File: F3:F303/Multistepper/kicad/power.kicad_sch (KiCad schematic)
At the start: 22 parts, among them J10 Screw_Terminal_01x02, Q2 IRF9310, U4 LM4050A(b)EX3-3.3, U5 LM2576-5.0, U6 LM1117-3.3

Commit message: multistepper: cont
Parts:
- added JP4, JP5: SolderJumper_2_Bridged, Jumper:SolderJumper-2_P1.3mm_Open_TrianglePad1.0x1.5mm, symbol Jumper:SolderJumper_2_Bridged
- C13, C15, C18: footprint Capacitor_SMD:C_0603_1608Metric_Pad1.05x0.95mm_HandSolder -> Capacitor_SMD:C_0603_1608Metric_Pad1.08x0.95mm_HandSolder
- R19, R20: footprint Resistor_SMD:R_0603_1608Metric_Pad1.05x0.95mm_HandSolder -> Resistor_SMD:R_0603_1608Metric_Pad0.98x0.95mm_HandSolder
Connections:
- net +5V: now also JP4.1 (A), JP5.1 (A); no longer C15.1, R20.2, U6.3 (VI)
- new net: C15.1, JP5.2 (B), U6.3 (VI)
- new net: JP4.2 (B), R20.2
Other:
- moved on the sheet: C12, R20, U4

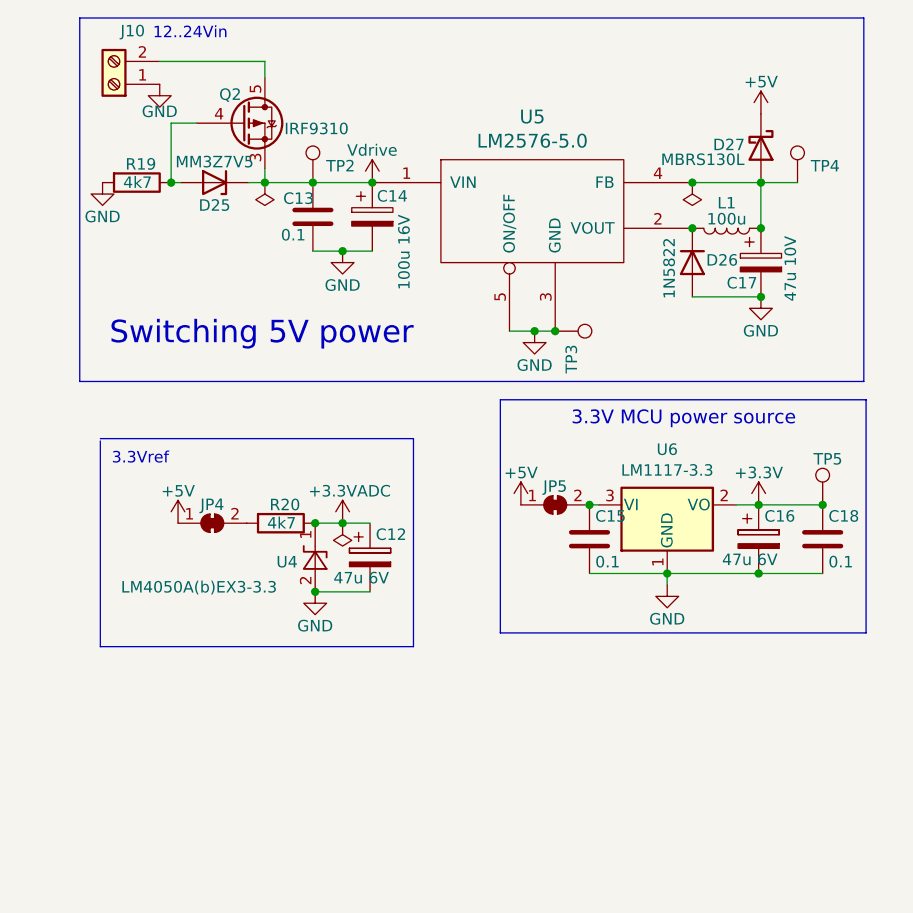
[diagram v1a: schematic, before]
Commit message: Multistepper PCB almost ready
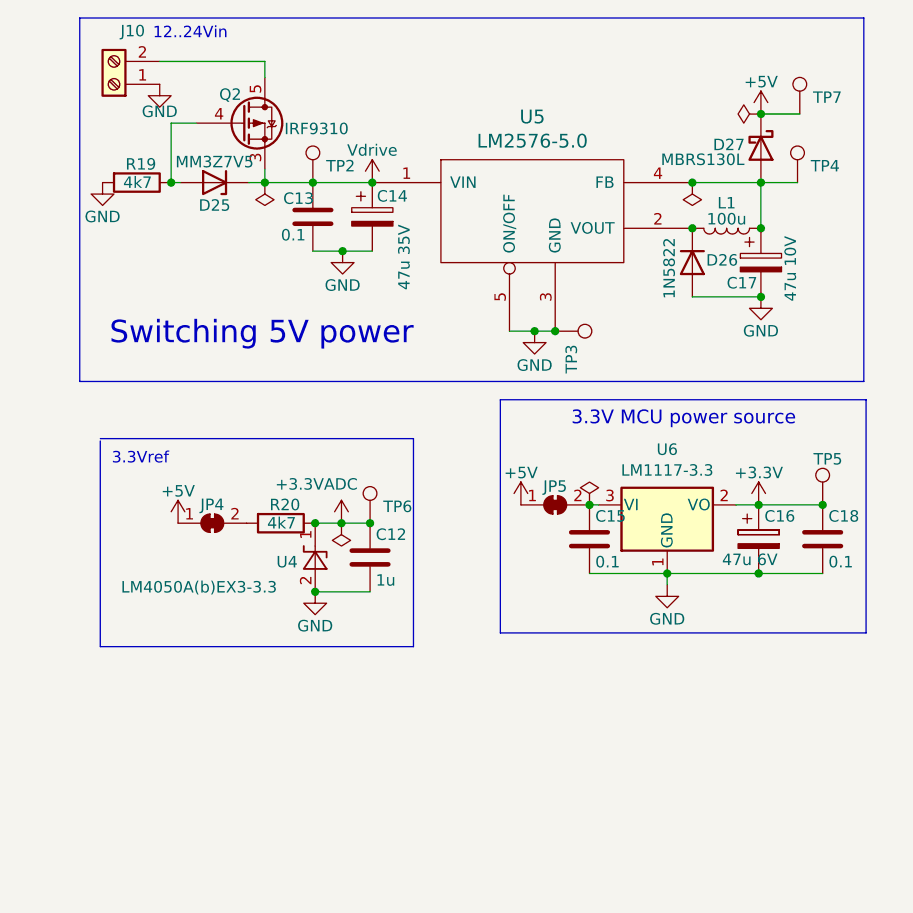
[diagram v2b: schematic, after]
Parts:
- removed C12: 47u 6V, Capacitor_Tantalum_SMD:CP_EIA-3216-18_Kemet-A_Pad1.58x1.35mm_HandSolder, symbol stm32-rescue:CP
- added C12: 1u, Capacitor_SMD:C_0603_1608Metric_Pad1.08x0.95mm_HandSolder, symbol stm32-rescue:C
- added TP6: 3V3ADC, TestPoint:TestPoint_THTPad_1.5x1.5mm_Drill0.7mm, symbol Connector:TestPoint
- added TP7: 5V, TestPoint:TestPoint_THTPad_1.5x1.5mm_Drill0.7mm, symbol Connector:TestPoint
- C14: value 100u 16V -> 47u 35V; footprint Capacitor_THT:CP_Radial_D8.0mm_P3.50mm -> Capacitor_Tantalum_SMD:CP_EIA-6032-28_Kemet-C_Pad2.25x2.35mm_HandSolder
- JP4: value SolderJumper_2_Bridged -> 3V3ADC
- JP5: value SolderJumper_2_Bridged -> 3V3
- TP2: value 5V -> Vin
- TP4: value 5V -> 5Vext
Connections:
- net +3.3VADC: now also C12.1, TP6.1
- net +5V: now also TP7.1
- net GND: now also C12.2
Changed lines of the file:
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@@
   (junction (at 87.376 36.068) (diameter 0) (color 0 0 0 0)
   )
+  (junction (at 48.387 73.914) (diameter 0) (color 0 0 0 0)
+  )
   (junction (at 29.464 36.068) (diameter 0) (color 0 0 0 0)
   )
@@
   (junction (at 51.816 36.068) (diameter 0) (color 0 0 0 0)
   )
-  (junction (at 48.514 73.914) (diameter 0) (color 0 0 0 0)
+  (junction (at 51.562 73.914) (diameter 0) (color 0 0 0 0)
   )
   (junction (at 84.582 79.502) (diameter 0) (color 0 0 0 0)
@@
   (junction (at 48.514 43.688) (diameter 0) (color 0 0 0 0)
   )
+  (junction (at 94.996 28.448) (diameter 0) (color 0 0 0 0)
+  )
   (junction (at 87.376 41.148) (diameter 0) (color 0 0 0 0)
   )
@@
     (stroke (width 0) (type default) (color 0 0 0 0))
   )
-  (wire (pts (xy 51.562 73.914) (xy 48.514 73.914))
+  (wire (pts (xy 45.466 73.914) (xy 48.387 73.914))
     (stroke (width 0) (type default) (color 0 0 0 0))
   )
@@
     (stroke (width 0) (type default) (color 0 0 0 0))
   )
-  (wire (pts (xy 48.514 73.914) (xy 48.514 73.66))
+  (wire (pts (xy 99.314 28.448) (xy 94.996 28.448))
     (stroke (width 0) (type default) (color 0 0 0 0))
   )
@@
     (stroke (width 0) (type default) (color 0 0 0 0))
   )
-  (wire (pts (xy 45.466 73.914) (xy 48.514 73.914))
+  (wire (pts (xy 48.387 73.914) (xy 51.562 73.914))
     (stroke (width 0) (type default) (color 0 0 0 0))
   )
@@
   (text "12..24Vin" (at 27.432 20.32 0)
     (effects (font (size 1.27 1.27)) (justify left bottom))
-  )
-  (symbol (lib_id "stm32-rescue:CP") (at 51.562 77.724 0) (unit 1)
-    (in_bom yes) (on_board yes)
-    (property "Reference" "C12" (id 0) (at 52.197 75.184 0)
-      (effects (font (size 1.27 1.27)) (justify left))
-    )
-    (property "Value" "47u 6V" (id 1) (at 47.498 80.01 0)
-      (effects (font (size 1.27 1.27)) (justify left))
-    )
-    (property "Footprint" "Capacitor_Tantalum_SMD:CP_EIA-3216-18_Kemet-A_Pad1.58x1.35mm_HandSolder" (id 2) (at 52.5272 81.534 0)
-      (effects (font (size 1.27 1.27)) hide)
-    )
-    (property "Datasheet" "" (id 3) (at 51.562 77.724 0))
-    (pin "1")
-    (pin "2")
   )
   (symbol (lib_id "elements:IRF9310") (at 37.338 29.464 0) (unit 1)
@@
     (pin "8")
   )
-  (symbol (lib_id "stm32-rescue:PWR_FLAG") (at 48.514 73.914 180) (unit 1)
-    (in_bom yes) (on_board yes)
-    (property "Reference" "#FLG01" (id 0) (at 48.514 76.327 0)
-      (effects (font (size 1.27 1.27)) hide)
-    )
-    (property "Value" "PWR_FLAG" (id 1) (at 48.514 78.486 0)
-      (effects (font (size 1.27 1.27)) hide)
-    )
-    (property "Footprint" "" (id 2) (at 48.514 73.914 0))
-    (property "Datasheet" "" (id 3) (at 48.514 73.914 0))
+  (symbol (lib_id "stm32-rescue:PWR_FLAG") (at 48.387 73.914 180) (unit 1)
+    (in_bom yes) (on_board yes)
+    (property "Reference" "#FLG01" (id 0) (at 48.387 76.327 0)
+      (effects (font (size 1.27 1.27)) hide)
+    )
+    (property "Value" "PWR_FLAG" (id 1) (at 48.387 78.486 0)
+      (effects (font (size 1.27 1.27)) hide)
+    )
+    (property "Footprint" "" (id 2) (at 48.387 73.914 0))
+    (property "Datasheet" "" (id 3) (at 48.387 73.914 0))
     (pin "1")
   )
@@
     (in_bom yes) (on_board yes) (fields_autoplaced)
     (property "Reference" "JP5" (id 0) (at 72.136 69.8302 0))
-    (property "Value" "SolderJumper_2_Bridged" (id 1) (at 72.136 69.8301 0)
+    (property "Value" "3V3" (id 1) (at 72.136 69.8301 0)
       (effects (font (size 1.27 1.27)) hide)
     )
@@
     (pin "1")
   )
-  (symbol (lib_id "power:+3.3VADC") (at 48.514 73.914 0) (mirror y) (unit 1)
-    (in_bom yes) (on_board yes)
-    (property "Reference" "#PWR028" (id 0) (at 44.704 75.184 0)
-      (effects (font (size 1.27 1.27)) hide)
-    )
-    (property "Value" "+3.3VADC" (id 1) (at 44.704 70.358 0)
+  (symbol (lib_id "power:+3.3VADC") (at 48.387 73.914 0) (mirror y) (unit 1)
+    (in_bom yes) (on_board yes)
+    (property "Reference" "#PWR028" (id 0) (at 44.577 75.184 0)
+      (effects (font (size 1.27 1.27)) hide)
+    )
+    (property "Value" "+3.3VADC" (id 1) (at 41.021 69.596 0)
       (effects (font (size 1.27 1.27)) (justify right))
     )
-    (property "Footprint" "" (id 2) (at 48.514 73.914 0)
-      (effects (font (size 1.27 1.27)) hide)
-    )
-    (property "Datasheet" "" (id 3) (at 48.514 73.914 0)
+    (property "Footprint" "" (id 2) (at 48.387 73.914 0)
+      (effects (font (size 1.27 1.27)) hide)
+    )
+    (property "Datasheet" "" (id 3) (at 48.387 73.914 0)
       (effects (font (size 1.27 1.27)) hide)
     )
@@
     (pin "1")
   )
+  (symbol (lib_id "power:PWR_FLAG") (at 94.996 28.448 90) (unit 1)
+    (in_bom yes) (on_board yes) (fields_autoplaced)
+    (property "Reference" "#FLG0102" (id 0) (at 93.091 28.448 0)
+      (effects (font (size 1.27 1.27)) hide)
+    )
+    (property "Value" "PWR_FLAG" (id 1) (at 91.4202 28.448 0)
+      (effects (font (size 1.27 1.27)) hide)
+    )
+    (property "Footprint" "" (id 2) (at 94.996 28.448 0)
+      (effects (font (size 1.27 1.27)) hide)
+    )
+    (property "Datasheet" "~" (id 3) (at 94.996 28.448 0)
+      (effects (font (size 1.27 1.27)) hide)
+    )
+    (pin "1")
+  )
   (symbol (lib_id "Connector:Screw_Terminal_01x02") (at 23.114 25.146 180) (unit 1)
     (in_bom yes) (on_board yes)
@@
     (pin "2")
   )
+  (symbol (lib_id "stm32-rescue:C") (at 51.562 77.724 0) (unit 1)
+    (in_bom yes) (on_board yes)
+    (property "Reference" "C12" (id 0) (at 52.197 75.184 0)
+      (effects (font (size 1.27 1.27)) (justify left))
+    )
+    (property "Value" "1u" (id 1) (at 52.197 80.264 0)
+      (effects (font (size 1.27 1.27)) (justify left))
+    )
+    (property "Footprint" "Capacitor_SMD:C_0603_1608Metric_Pad1.08x0.95mm_HandSolder" (id 2) (at 52.5272 81.534 0)
+      (effects (font (size 1.27 1.27)) hide)
+    )
+    (property "Datasheet" "" (id 3) (at 51.562 77.724 0))
+    (pin "1")
+    (pin "2")
+  )
   (symbol (lib_id "Connector:TestPoint") (at 99.06 36.068 0) (unit 1)
     (in_bom yes) (on_board yes)
@@
       (effects (font (size 1.27 1.27)) (justify left))
     )
-    (property "Value" "5V" (id 1) (at 100.5332 35.3822 0)
+    (property "Value" "5Vext" (id 1) (at 100.5332 35.3822 0)
       (effects (font (size 1.27 1.27)) (justify left) hide)
     )
@@
     (in_bom yes) (on_board yes) (fields_autoplaced)
     (property "Reference" "JP4" (id 0) (at 34.036 71.8622 0))
-    (property "Value" "SolderJumper_2_Bridged" (id 1) (at 34.036 71.8621 0)
+    (property "Value" "3V3ADC" (id 1) (at 34.036 71.8621 0)
       (effects (font (size 1.27 1.27)) hide)
     )
@@
     )
     (property "Datasheet" "" (id 3) (at 21.844 36.068 0)
+      (effects (font (size 1.27 1.27)) hide)
+    )
+    (pin "1")
+  )
+  (symbol (lib_id "Connector:TestPoint") (at 99.314 28.448 0) (unit 1)
+    (in_bom yes) (on_board yes)
+    (property "Reference" "TP7" (id 0) (at 100.7872 26.6192 0)
+      (effects (font (size 1.27 1.27)) (justify left))
+    )
+    (property "Value" "5V" (id 1) (at 100.7872 27.7622 0)
+      (effects (font (size 1.27 1.27)) (justify left) hide)
+    )
+    (property "Footprint" "TestPoint:TestPoint_THTPad_1.5x1.5mm_Drill0.7mm" (id 2) (at 104.394 28.448 0)
+      (effects (font (size 1.27 1.27)) hide)
+    )
+    (property "Datasheet" "~" (id 3) (at 104.394 28.448 0)
       (effects (font (size 1.27 1.27)) hide)
     )
@@
     (pin "1")
   )
+  (symbol (lib_id "power:PWR_FLAG") (at 75.946 71.882 0) (unit 1)
+    (in_bom yes) (on_board yes) (fields_autoplaced)
+    (property "Reference" "#FLG0101" (id 0) (at 75.946 69.977 0)
+      (effects (font (size 1.27 1.27)) hide)
+    )
+    (property "Value" "PWR_FLAG" (id 1) (at 75.946 68.3062 0)
+      (effects (font (size 1.27 1.27)) hide)
+    )
+    (property "Footprint" "" (id 2) (at 75.946 71.882 0)
+      (effects (font (size 1.27 1.27)) hide)
+    )
+    (property "Datasheet" "~" (id 3) (at 75.946 71.882 0)
+      (effects (font (size 1.27 1.27)) hide)
+    )
+    (pin "1")
+  )
   (symbol (lib_id "Connector:TestPoint") (at 45.212 36.068 0) (unit 1)
     (in_bom yes) (on_board yes)
@@
       (effects (font (size 1.27 1.27)) (justify left))
     )
-    (property "Value" "5V" (id 1) (at 46.6852 35.3822 0)
+    (property "Value" "Vin" (id 1) (at 46.6852 35.3822 0)
       (effects (font (size 1.27 1.27)) (justify left) hide)
     )
@@
       (effects (font (size 1.27 1.27)) (justify left))
     )
-    (property "Value" "100u 16V" (id 1) (at 55.372 48.006 90)
-      (effects (font (size 1.27 1.27)) (justify left))
-    )
-    (property "Footprint" "Capacitor_THT:CP_Radial_D8.0mm_P3.50mm" (id 2) (at 52.7812 43.688 0)
+    (property "Value" "47u 35V" (id 1) (at 55.372 48.006 90)
+      (effects (font (size 1.27 1.27)) (justify left))
+    )
+    (property "Footprint" "Capacitor_Tantalum_SMD:CP_EIA-6032-28_Kemet-C_Pad2.25x2.35mm_HandSolder" (id 2) (at 52.7812 43.688 0)
       (effects (font (size 1.27 1.27)) hide)
     )
@@
       (effects (font (size 1.27 1.27)) hide)
     )
+    (pin "1")
+  )
+  (symbol (lib_id "Connector:TestPoint") (at 51.562 73.914 0) (unit 1)
+    (in_bom yes) (on_board yes)
+    (property "Reference" "TP6" (id 0) (at 53.0352 72.0852 0)
+      (effects (font (size 1.27 1.27)) (justify left))
+    )
+    (property "Value" "3V3ADC" (id 1) (at 53.0352 73.2282 0)
+      (effects (font (size 1.27 1.27)) (justify left) hide)
+    )
+    (property "Footprint" "TestPoint:TestPoint_THTPad_1.5x1.5mm_Drill0.7mm" (id 2) (at 56.642 73.914 0)
+      (effects (font (size 1.27 1.27)) hide)
+    )
+    (property "Datasheet" "~" (id 3) (at 56.642 73.914 0)
+      (effects (font (size 1.27 1.27)) hide)
+    )
